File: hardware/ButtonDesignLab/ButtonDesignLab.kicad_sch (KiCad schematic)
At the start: 2 parts

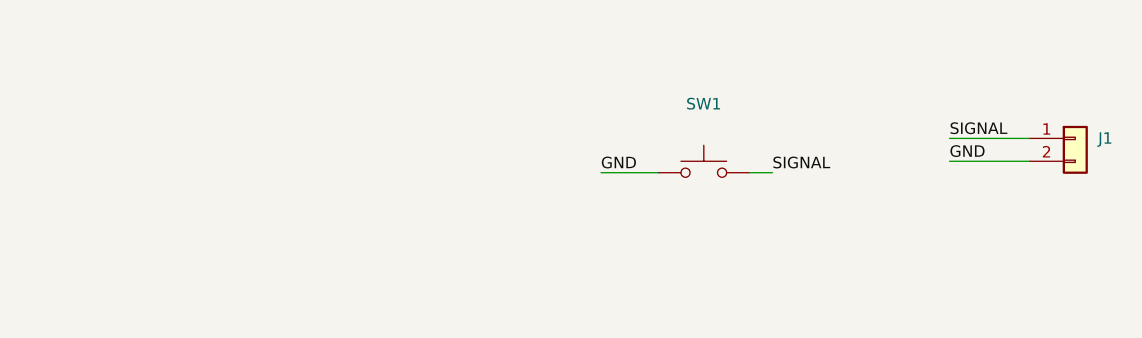
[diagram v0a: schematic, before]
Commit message: Almost finished the PCB  and started with the PCB of buttons
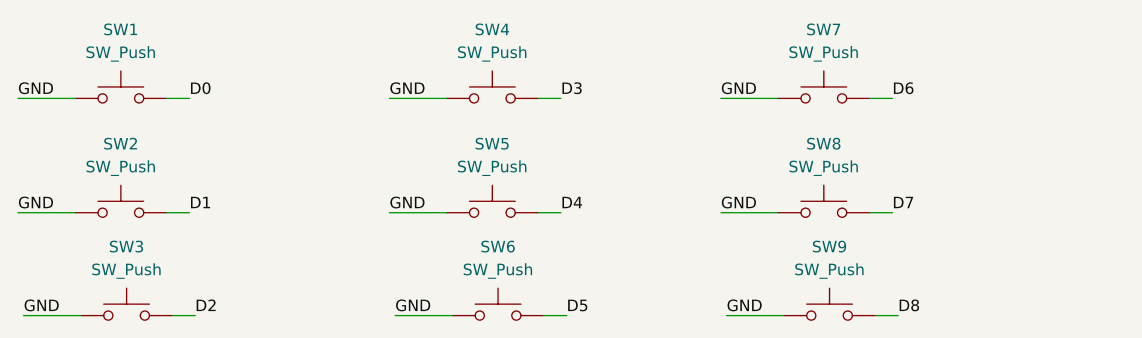
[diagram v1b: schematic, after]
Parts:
- removed J1: (no value), symbol Connector_Generic:Conn_01x02
- added SW2, SW3, SW4, SW5, SW6, SW7, SW8, SW9: SW_Push, Design:Button, symbol Switch:SW_Push
- SW1: value (none) -> SW_Push; footprint (none) -> Design:Button
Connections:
- net GND: now also SW2.1, SW3.1, SW4.1, SW5.1, SW6.1, SW7.1, SW8.1, SW9.1
- net SIGNAL renamed D0
- new net D1: SW2.2
- new net D2: SW3.2
- new net D3: SW4.2
- new net D4: SW5.2
- new net D5: SW6.2
- new net D6: SW7.2
- new net D7: SW8.2
- new net D8: SW9.2
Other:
- moved on the sheet: SW1

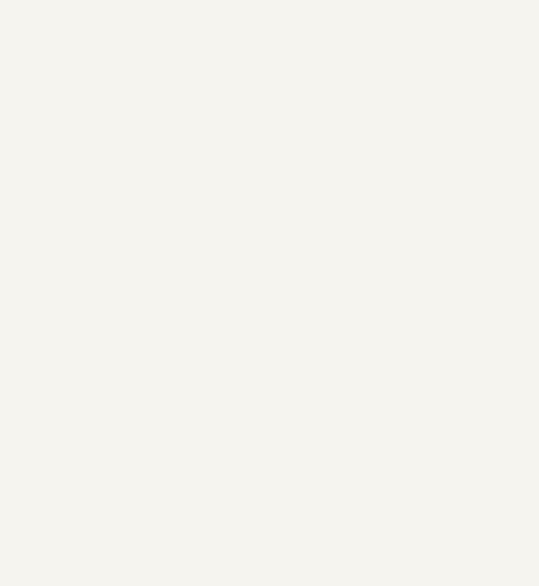
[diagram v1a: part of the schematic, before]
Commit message: Finished button PCBs
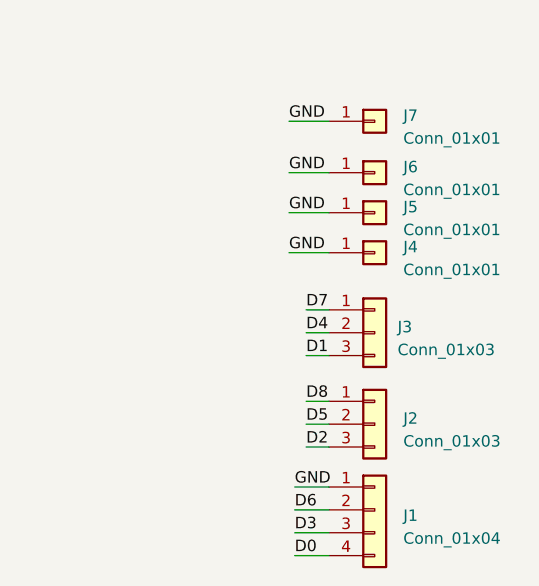
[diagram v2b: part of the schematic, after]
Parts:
- added J1: Conn_01x04, Connector_PinHeader_2.54mm:PinHeader_1x04_P2.54mm_Vertical, symbol Connector_Generic:Conn_01x04
- added J2, J3: Conn_01x03, Connector_PinHeader_2.54mm:PinHeader_1x03_P2.54mm_Vertical, symbol Connector_Generic:Conn_01x03
- added J4, J5, J6, J7: Conn_01x01, Connector_PinHeader_2.54mm:PinHeader_1x01_P2.54mm_Vertical, symbol Connector_Generic:Conn_01x01
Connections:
- net D0: now also J1.4 (Pin_4)
- net D1: now also J3.3 (Pin_3)
- net D2: now also J2.3 (Pin_3)
- net D3: now also J1.3 (Pin_3)
- net D4: now also J3.2 (Pin_2)
- net D5: now also J2.2 (Pin_2)
- net D6: now also J1.2 (Pin_2)
- net D7: now also J3.1 (Pin_1)
- net D8: now also J2.1 (Pin_1)
- net GND: now also J1.1 (Pin_1), J4.1 (Pin_1), J5.1 (Pin_1), J6.1 (Pin_1), J7.1 (Pin_1)
